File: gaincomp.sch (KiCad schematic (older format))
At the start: 22 parts

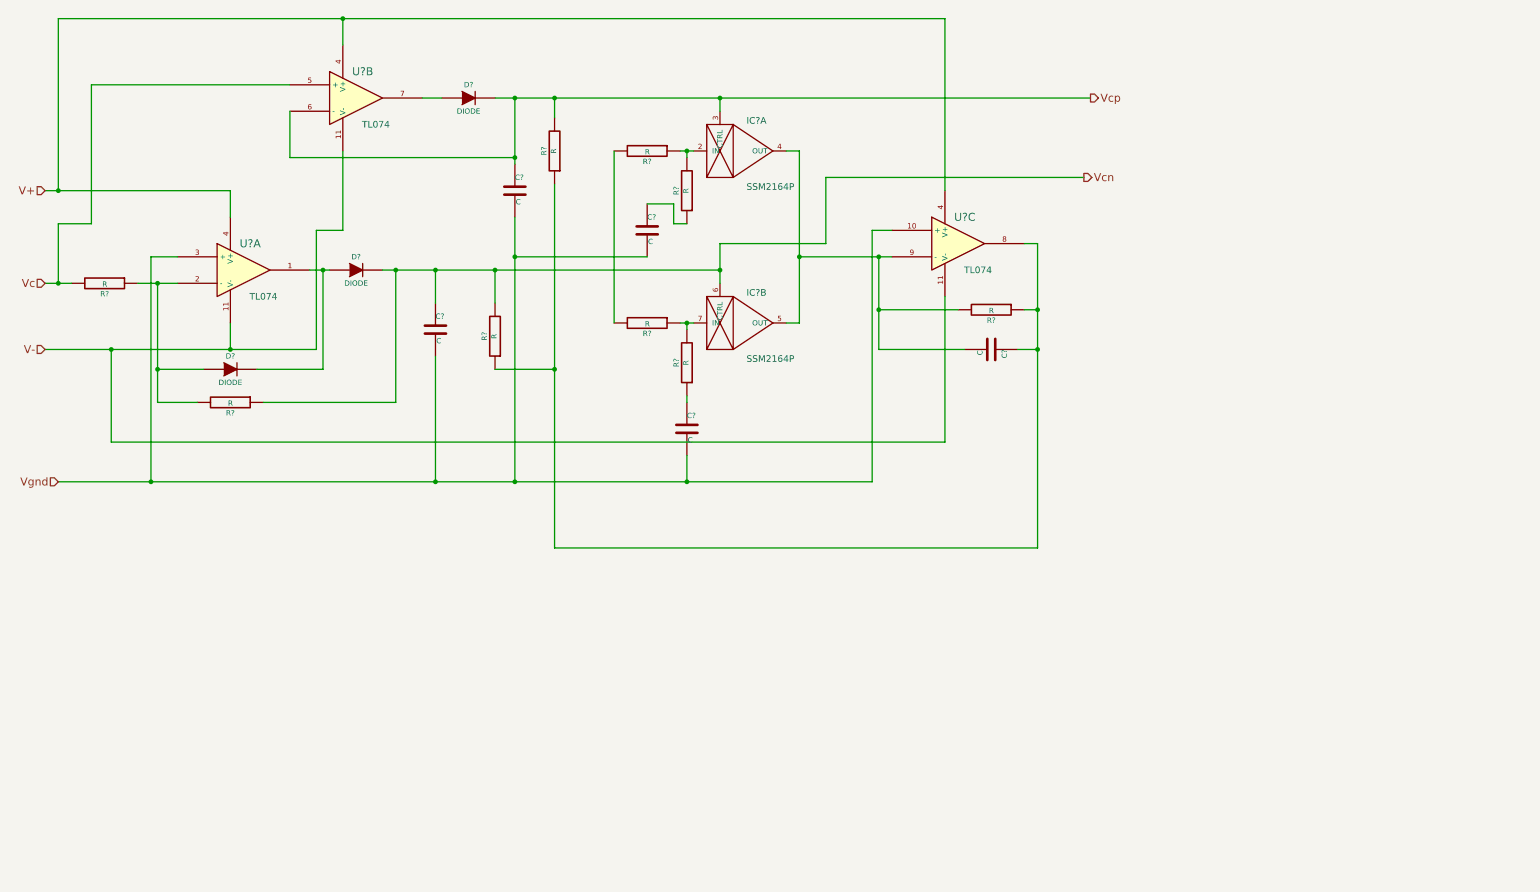
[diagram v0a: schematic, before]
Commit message: Added top-level connections
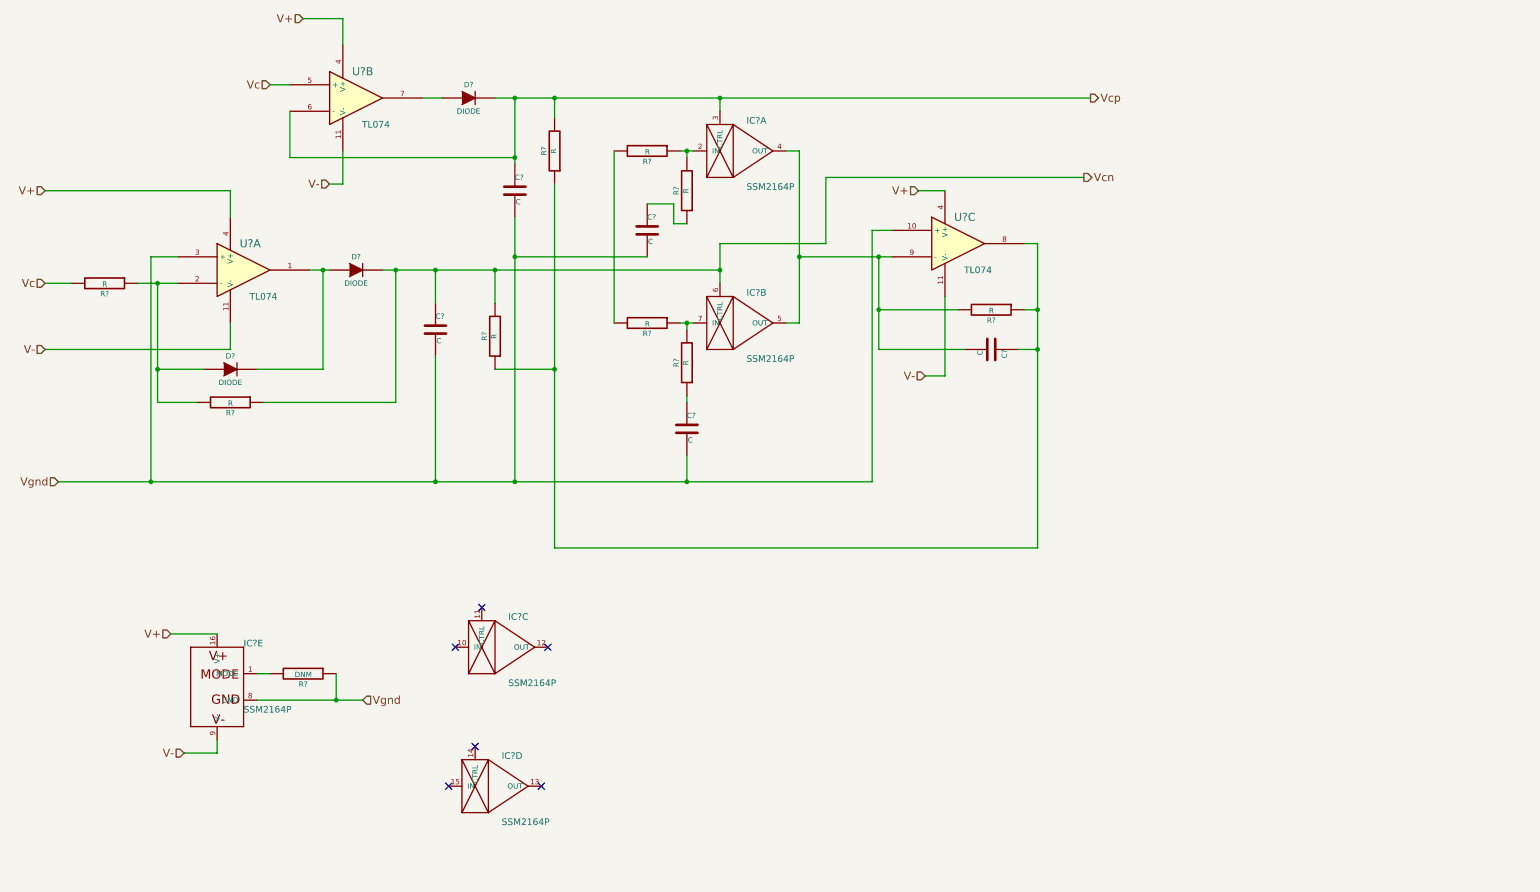
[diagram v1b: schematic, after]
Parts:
- added IC? (x3): SSM2164P, ssm2164-DIL16, symbol SSM2164P
- added R?: DNM, symbol R
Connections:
- net V+: now also IC?.16 (V+)
- net V-: now also IC?.9 (V-)
- net Vgnd: now also IC?.8 (GND), R?.1
- new net: IC?.1 (MODE), R?.2
- no-connect marks 0 -> 6
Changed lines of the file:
@@
 $Descr A4 11693 8268
 encoding utf-8
-Sheet 4 6
+Sheet 4 9
 Title ""
 Date ""
@@
 	2600 2000 2600 2200
 Wire Wire Line
-	1200 3200 3250 3200
-Wire Wire Line
 	2600 3200 2600 3000
 Wire Wire Line
@@
 	1200 2700 1400 2700
 Wire Wire Line
-	1300 2000 1300 700
-Wire Wire Line
 	3450 700  3450 900
-Connection ~ 1300 2000
-Wire Wire Line
-	3250 3200 3250 2300
-Wire Wire Line
-	3250 2300 3450 2300
-Wire Wire Line
-	3450 2300 3450 1700
-Connection ~ 2600 3200
-Wire Wire Line
-	1300 2700 1300 2250
-Wire Wire Line
-	1300 2250 1550 2250
-Wire Wire Line
-	1550 2250 1550 1200
-Wire Wire Line
-	1550 1200 3050 1200
-Connection ~ 1300 2700
 Wire Wire Line
 	4050 1300 4200 1300
@@
 Wire Wire Line
 	6900 3000 6800 3000
-Wire Wire Line
-	8000 700  8000 2000
-Connection ~ 3450 700
-Wire Wire Line
-	8000 2800 8000 3900
-Wire Wire Line
-	8000 3900 1700 3900
-Wire Wire Line
-	1700 3900 1700 3200
-Connection ~ 1700 3200
 Wire Wire Line
 	7600 2500 6900 2500
@@
 Connection ~ 5050 3350
 Connection ~ 8700 3200
-Wire Wire Line
-	1300 700  8000 700
 Connection ~ 6300 1300
 Wire Wire Line
@@
 Wire Wire Line
 	5500 1700 5500 3000
+Text HLabel 2900 1200 0    60   Input ~ 0
+Vc
+Wire Wire Line
+	2900 1200 3050 1200
+Text HLabel 7850 3400 0    60   Input ~ 0
+V-
+Wire Wire Line
+	7850 3400 8000 3400
+Wire Wire Line
+	8000 3400 8000 2800
+Wire Wire Line
+	1200 3200 2600 3200
+Text HLabel 3350 1950 0    60   Input ~ 0
+V-
+Wire Wire Line
+	3350 1950 3450 1950
+Wire Wire Line
+	3450 1950 3450 1700
+Text HLabel 3150 700  0    60   Input ~ 0
+V+
+Wire Wire Line
+	3150 700  3450 700
+Text HLabel 7800 2000 0    60   Input ~ 0
+V+
+Wire Wire Line
+	7800 2000 8000 2000
+$Comp
+L SSM2164P IC?
+U 3 1 5462C12D
+P 4500 5450
+F 0 "IC?" H 4700 5650 50  0000 L BNN
+F 1 "SSM2164P" H 4700 5150 50  0000 L BNN
+F 2 "ssm2164-DIL16" H 4500 5600 50  0001 C CNN
+F 3 "" H 4500 5450 60  0000 C CNN
+	3    4500 5450
+	1    0    0    -1
+$EndComp
+$Comp
+L SSM2164P IC?
+U 4 1 5462C1A4
+P 4450 6500
+F 0 "IC?" H 4650 6700 50  0000 L BNN
+F 1 "SSM2164P" H 4650 6200 50  0000 L BNN
+F 2 "ssm2164-DIL16" H 4450 6650 50  0001 C CNN
+F 3 "" H 4450 6500 60  0000 C CNN
+	4    4450 6500
+	1    0    0    -1
+$EndComp
+$Comp
+L SSM2164P IC?
+U 5 1 5462C219
+P 2500 5650
+F 0 "IC?" H 2700 5850 50  0000 L BNN
+F 1 "SSM2164P" H 2700 5350 50  0000 L BNN
+F 2 "ssm2164-DIL16" H 2500 5800 50  0001 C CNN
+F 3 "" H 2500 5650 60  0000 C CNN
+	5    2500 5650
+	1    0    0    -1
+$EndComp
+Text HLabel 3600 5850 2    60   Input ~ 0
+Vgnd
+Text HLabel 2250 6250 0    60   Input ~ 0
+V-
+Text HLabel 2150 5350 0    60   Input ~ 0
+V+
+Wire Wire Line
+	2150 5350 2500 5350
+Wire Wire Line
+	2250 6250 2500 6250
+Wire Wire Line
+	2500 6250 2500 6150
+Wire Wire Line
+	2800 5850 3600 5850
+NoConn ~ 4300 5450
+NoConn ~ 4500 5150
+NoConn ~ 5000 5450
+NoConn ~ 4950 6500
+NoConn ~ 4450 6200
+NoConn ~ 4250 6500
+$Comp
+L R R?
+U 1 1 5462C5A9
+P 3150 5650
+F 0 "R?" V 3230 5650 40  0000 C CNN
+F 1 "DNM" V 3157 5651 40  0000 C CNN
+F 2 "" V 3080 5650 30  0000 C CNN
+F 3 "" H 3150 5650 30  0000 C CNN
+	1    3150 5650
+	0    1    1    0
+$EndComp
+Wire Wire Line
+	3400 5650 3400 5850
+Connection ~ 3400 5850
+Wire Wire Line
+	2900 5650 2800 5650
 $EndSCHEMATC

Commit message: Some work
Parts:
- removed C? (x5): C, symbol C
- removed D? (x3): DIODE, symbol DIODE
- removed IC? (x3): SSM2164P, ssm2164-DIL16, symbol SSM2164P
- removed R? (x9): R, symbol R
- removed U? (x3): TL074, symbol TL074
- added C? (x2): C, symbol C
- added C? (x2): 560p, symbol C
- added C?: 100p, symbol C
- added D? (x3): DIODE, symbol DIODE
- added IC? (x3): SSM2164P, ssm2164-DIL16, symbol SSM2164P
- added R? (x2): 100k, symbol R
- added R? (x3): 80k, symbol R
- added R? (x2): 500, symbol R
- added R? (x3): 33k, symbol R
- added U? (x5): TL074, symbol TL074
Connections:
- net V+: now also IC?.16 (V+), R?.1, U?.4 (V+), U?.4 (V+), U?.4 (V+), U?.4 (V+), U?.4 (V+)
- net V-: now also IC?.9 (V-), R?.2, R?.2, U?.11 (V-), U?.11 (V-), U?.11 (V-), U?.11 (V-), U?.11 (V-)
- net Vc: now also R?.2, U?.5 (+)
- net Vcn: now also IC?.6 (CTRL), U?.13 (-), U?.14
- net Vcp: now also IC?.3 (CTRL), U?.1, U?.2 (-)
- net Vgnd: now also C?.2, C?.2, C?.2, C?.2, IC?.8 (GND), U?.10 (+), U?.5 (+)
- net at R?.2: now also IC?.1 (MODE)
- new net: C?.1, D?.2 (K), R?.2, U?.3 (+), U?.6 (-)
- new net: D?.1 (A), U?.7
- new net: D?.1 (A), R?.1, R?.2, U?.9 (-)
- new net: D?.1 (A), D?.2 (K), U?.8
- new net: C?.1, D?.2 (K), R?.1, R?.2, U?.12 (+)
- new net: C?.1, R?.1 (x2)
- new net: IC?.2 (IN), R?.1, R?.2
- new net: C?.2, IC?.4 (OUT), IC?.5 (OUT), R?.2, R?.2, U?.6 (-)
- new net: IC?.7 (IN), R?.1, R?.2
- new net vo: C?.1, R?.1, R?.1, R?.1, U?.7
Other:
- note added: "This resistor adds bias current, so that when the gain is 1, the\ncurrent seen by the amp below is 0.\nio = ii * 10^(-2/3vc)"
- note added: "When used as feedback, the gain here can be\nincreased (increase the 33k resistor)."
- note added: "vo > 0V"
- moved on the sheet: IC?C, IC?D, R?

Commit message: Ready for tapeout
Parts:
- added R15, R16: 100k, symbol R
- R17, R18: renamed from R?; value 33k -> 100k
- gave numbers to parts that had none: 20
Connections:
- net Vcn: now also U4.1, U4.2 (-); no longer U4.13 (-), U4.14
- net Vcp: now also U1.13 (-), U1.14; no longer U1.1, U1.2 (-)
- net at C19.1, D3.2 (K), U1.6 (-): now also R15.1; no longer R17.2, U1.3 (+)
- net at C20.1, D4.2 (K), R13.1: now also R16.1; no longer R18.2, U4.12 (+)
- new net: R15.2, R17.2, U1.12 (+)
- new net: R16.2, R18.2, U4.3 (+)
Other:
- note added: "-10V to +10V"
- note added: "This resistor adds bias current, so that when the gain is 1, the\ncurrent seen by the amp below is 0.\nio = ii * 10^(-2/3vc). Increase resistor to lower gain."
- note removed: "This resistor adds bias current, so that when the gain is 1, the\ncurrent seen by the amp below is 0.\nio = ii * 10^(-2/3vc)"
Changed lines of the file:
@@
 $Descr A4 11693 8268
 encoding utf-8
-Sheet 4 9
+Sheet 4 10
 Title ""
 Date ""
@@
 Vcn
 $Comp
-L SSM2164P IC?
+L SSM2164P IC1
 U 3 1 5462C12D
 P 3050 6900
-F 0 "IC?" H 3250 7100 50  0000 L BNN
+F 0 "IC1" H 3250 7100 50  0000 L BNN
 F 1 "SSM2164P" H 3250 6600 50  0000 L BNN
 F 2 "ssm2164-DIL16" H 3050 7050 50  0001 C CNN
@@
 $EndComp
 $Comp
-L SSM2164P IC?
+L SSM2164P IC1
 U 4 1 5462C1A4
 P 5100 6650
-F 0 "IC?" H 5300 6850 50  0000 L BNN
+F 0 "IC1" H 5300 6850 50  0000 L BNN
 F 1 "SSM2164P" H 5300 6350 50  0000 L BNN
 F 2 "ssm2164-DIL16" H 5100 6800 50  0001 C CNN
@@
 NoConn ~ 4900 6650
 $Comp
-L R R?
+L R R14
 U 1 1 5462C5A9
 P 3800 5800
-F 0 "R?" V 3880 5800 40  0000 C CNN
+F 0 "R14" V 3880 5800 40  0000 C CNN
 F 1 "DNM" V 3807 5801 40  0000 C CNN
 F 2 "" V 3730 5800 30  0000 C CNN
@@
 $EndComp
 $Comp
-L TL074 U?
+L TL074 U1
 U 2 1 54A69C55
 P 2850 1550
-F 0 "U?" H 2900 1750 60  0000 C CNN
+F 0 "U1" H 2900 1750 60  0000 C CNN
 F 1 "TL074" H 3000 1350 50  0000 C CNN
 F 2 "" H 2850 1550 60  0000 C CNN
@@
 $EndComp
 $Comp
-L DIODE D?
+L DIODE D3
 U 1 1 54A69C67
 P 3750 1550
-F 0 "D?" H 3750 1650 40  0000 C CNN
+F 0 "D3" H 3750 1650 40  0000 C CNN
 F 1 "DIODE" H 3750 1450 40  0000 C CNN
 F 2 "" H 3750 1550 60  0000 C CNN
@@
 $EndComp
 $Comp
-L R R?
+L R R12
 U 1 1 54A69D4C
 P 1900 3250
-F 0 "R?" V 1980 3250 40  0000 C CNN
+F 0 "R12" V 1980 3250 40  0000 C CNN
 F 1 "100k" V 1907 3251 40  0000 C CNN
 F 2 "" V 1830 3250 30  0000 C CNN
@@
 V-
 $Comp
-L DIODE D?
+L DIODE D2
 U 1 1 54A69FAB
 P 2750 4100
-F 0 "D?" H 2750 4200 40  0000 C CNN
+F 0 "D2" H 2750 4200 40  0000 C CNN
 F 1 "DIODE" H 2750 4000 40  0000 C CNN
 F 2 "" H 2750 4100 60  0000 C CNN
@@
 $EndComp
 $Comp
-L R R?
+L R R13
 U 1 1 54A69FBB
 P 2750 4350
-F 0 "R?" V 2830 4350 40  0000 C CNN
+F 0 "R13" V 2830 4350 40  0000 C CNN
 F 1 "100k" V 2757 4351 40  0000 C CNN
 F 2 "" V 2680 4350 30  0000 C CNN
@@
 Vgnd
 $Comp
-L DIODE D?
+L DIODE D4
 U 1 1 54A6A594
 P 3750 3150
-F 0 "D?" H 3750 3250 40  0000 C CNN
+F 0 "D4" H 3750 3250 40  0000 C CNN
 F 1 "DIODE" H 3750 3050 40  0000 C CNN
 F 2 "" H 3750 3150 60  0000 C CNN
@@
 $EndComp
 $Comp
-L C C?
+L C C19
 U 1 1 54A6A72C
 P 4250 1850
-F 0 "C?" H 4250 1950 40  0000 L CNN
+F 0 "C19" H 4250 1950 40  0000 L CNN
 F 1 "C" H 4256 1765 40  0000 L CNN
 F 2 "" H 4288 1700 30  0000 C CNN
@@
 Vgnd
 $Comp
-L C C?
+L C C22
 U 1 1 54A6A84D
 P 7850 4450
-F 0 "C?" H 7850 4550 40  0000 L CNN
+F 0 "C22" H 7850 4550 40  0000 L CNN
 F 1 "560p" H 7856 4365 40  0000 L CNN
 F 2 "" H 7888 4300 30  0000 C CNN
@@
 $EndComp
 $Comp
-L SSM2164P IC?
+L SSM2164P IC1
 U 1 1 54A6AEA4
 P 8150 1950
-F 0 "IC?" H 8350 2150 50  0000 L BNN
+F 0 "IC1" H 8350 2150 50  0000 L BNN
 F 1 "SSM2164P" H 8350 1650 50  0000 L BNN
 F 2 "ssm2164-DIL16" H 8150 2100 50  0001 C CNN
@@
 $EndComp
 $Comp
-L SSM2164P IC?
+L SSM2164P IC1
 U 2 1 54A6AEAF
 P 8150 3550
-F 0 "IC?" H 8350 3750 50  0000 L BNN
+F 0 "IC1" H 8350 3750 50  0000 L BNN
 F 1 "SSM2164P" H 8350 3250 50  0000 L BNN
 F 2 "ssm2164-DIL16" H 8150 3700 50  0001 C CNN
@@
 $EndComp
 $Comp
-L R R?
+L R R19
 U 1 1 54A6B133
 P 7500 1950
-F 0 "R?" V 7580 1950 40  0000 C CNN
+F 0 "R19" V 7580 1950 40  0000 C CNN
 F 1 "80k" V 7507 1951 40  0000 C CNN
 F 2 "" V 7430 1950 30  0000 C CNN
@@
 $EndComp
 $Comp
-L R R?
+L R R21
 U 1 1 54A6B13E
 P 7850 2300
-F 0 "R?" V 7930 2300 40  0000 C CNN
+F 0 "R21" V 7930 2300 40  0000 C CNN
 F 1 "500" V 7857 2301 40  0000 C CNN
 F 2 "" V 7780 2300 30  0000 C CNN
@@
 $EndComp
 $Comp
-L R R?
+L R R20
 U 1 1 54A6B149
 P 7500 3550
-F 0 "R?" V 7580 3550 40  0000 C CNN
+F 0 "R20" V 7580 3550 40  0000 C CNN
 F 1 "80k" V 7507 3551 40  0000 C CNN
 F 2 "" V 7430 3550 30  0000 C CNN
@@
 $EndComp
 $Comp
-L R R?
+L R R22
 U 1 1 54A6B154
 P 7850 3900
-F 0 "R?" V 7930 3900 40  0000 C CNN
+F 0 "R22" V 7930 3900 40  0000 C CNN
 F 1 "500" V 7857 3901 40  0000 C CNN
 F 2 "" V 7780 3900 30  0000 C CNN
@@
 $EndComp
 $Comp
-L C C?
+L C C21
 U 1 1 54A6B15F
 P 7850 2850
-F 0 "C?" H 7850 2950 40  0000 L CNN
+F 0 "C21" H 7850 2950 40  0000 L CNN
 F 1 "560p" H 7856 2765 40  0000 L CNN
 F 2 "" H 7888 2700 30  0000 C CNN
@@
 $EndComp
 $Comp
-L C C?
+L C C20
 U 1 1 54A6B16A
 P 4250 3450
-F 0 "C?" H 4250 3550 40  0000 L CNN
+F 0 "C20" H 4250 3550 40  0000 L CNN
 F 1 "C" H 4256 3365 40  0000 L CNN
 F 2 "" H 4288 3300 30  0000 C CNN
@@
 Vgnd
 $Comp
-L TL074 U?
+L TL074 U1
 U 3 1 54A6B66B
 P 2850 3150
-F 0 "U?" H 2900 3350 60  0000 C CNN
+F 0 "U1" H 2900 3350 60  0000 C CNN
 F 1 "TL074" H 3000 2950 50  0000 C CNN
 F 2 "" H 2850 3150 60  0000 C CNN
@@
 Vgnd
 $Comp
-L R R?
+L R R24
 U 1 1 54A6BB31
 P 9900 4300
-F 0 "R?" V 9980 4300 40  0000 C CNN
+F 0 "R24" V 9980 4300 40  0000 C CNN
 F 1 "33k" V 9907 4301 40  0000 C CNN
 F 2 "" V 9830 4300 30  0000 C CNN
@@
 $EndComp
 $Comp
-L C C?
+L C C23
 U 1 1 54A6BB3C
 P 9900 4550
-F 0 "C?" V 10050 4550 40  0000 L CNN
+F 0 "C23" V 10050 4550 40  0000 L CNN
 F 1 "100p" V 9850 4650 40  0000 L CNN
 F 2 "" H 9938 4400 30  0000 C CNN
@@
 $EndComp
 $Comp
-L R R?
+L R R23
 U 1 1 54A6CBE5
 P 9200 1950
-F 0 "R?" V 9280 1950 40  0000 C CNN
+F 0 "R23" V 9280 1950 40  0000 C CNN
 F 1 "80k" V 9207 1951 40  0000 C CNN
 F 2 "" V 9130 1950 30  0000 C CNN
@@
 When used as feedback, the gain here can be\nincreased (increase the 33k resistor).
 Text Notes 8800 1800 0    60   ~ 0
-This resistor adds bias current, so that when the gain is 1, the\ncurrent seen by the amp below is 0.\nio = ii * 10^(-2/3vc)
+This resistor adds bias current, so that when the gain is 1, the\ncurrent seen by the amp below is 0.\nio = ii * 10^(-2/3vc). Increase resistor to lower gain.
 Text HLabel 9550 1950 2    60   Input ~ 0
 V+
@@
 V-
 $Comp
-L SSM2164P IC?
+L SSM2164P IC1
 U 5 1 54A92775
 P 3150 5800
-F 0 "IC?" H 3350 6000 50  0000 L BNN
+F 0 "IC1" H 3350 6000 50  0000 L BNN
 F 1 "SSM2164P" H 3350 5500 50  0000 L BNN
 F 2 "ssm2164-DIL16" H 3150 5950 50  0001 C CNN
@@
 V+
 $Comp
-L TL074 U?
-U 1 1 54A965B4
+L TL074 U1
+U 4 1 54A965B4
 P 6250 1550
-F 0 "U?" H 6300 1750 60  0000 C CNN
+F 0 "U1" H 6300 1750 60  0000 C CNN
 F 1 "TL074" H 6400 1350 50  0000 C CNN
 F 2 "" H 6250 1550 60  0000 C CNN
 F 3 "" H 6250 1550 60  0000 C CNN
-	1    6250 1550
-	1    0    0    -1
-$EndComp
-$Comp
-L TL074 U?
-U 4 1 54A965C8
+	4    6250 1550
+	1    0    0    -1
+$EndComp
+$Comp
+L TL074 U4
+U 1 1 54A965C8
 P 6250 3150
-F 0 "U?" H 6300 3350 60  0000 C CNN
+F 0 "U4" H 6300 3350 60  0000 C CNN
 F 1 "TL074" H 6400 2950 50  0000 C CNN
 F 2 "" H 6250 3150 60  0000 C CNN
 F 3 "" H 6250 3150 60  0000 C CNN
-	4    6250 3150
+	1    6250 3150
 	1    0    0    -1
 $EndComp
@@
 V-
 $Comp
-L R R?
+L R R17
 U 1 1 54A9638B
 P 4600 1900
-F 0 "R?" V 4680 1900 40  0000 C CNN
-F 1 "33k" V 4607 1901 40  0000 C CNN
+F 0 "R17" V 4680 1900 40  0000 C CNN
+F 1 "100k" V 4607 1901 40  0000 C CNN
 F 2 "" V 4530 1900 30  0000 C CNN
 F 3 "" H 4600 1900 30  0000 C CNN
@@
 	-1   0    0    1
 $EndComp
+$Comp
+L R R18
+U 1 1 54B11176
+P 4600 3500
+F 0 "R18" V 4680 3500 40  0000 C CNN
+F 1 "100k" V 4607 3501 40  0000 C CNN
+F 2 "" V 4530 3500 30  0000 C CNN
+F 3 "" H 4600 3500 30  0000 C CNN
+	1    4600 3500
+	-1   0    0    1
+$EndComp
+Text HLabel 7150 3550 0    60   Input ~ 0
+V-
+$Comp
+L TL074 U4
+U 2 1 54FF9680
+P 10000 3450
+F 0 "U4" H 10050 3650 60  0000 C CNN
+F 1 "TL074" H 10150 3250 50  0000 C CNN
+F 2 "" H 10000 3450 60  0000 C CNN
+F 3 "" H 10000 3450 60  0000 C CNN
+	2    10000 3450
+	1    0    0    -1
+$EndComp
+$Comp
+L R R15
+U 1 1 5504F2C8
+P 4350 1200
+F 0 "R15" V 4430 1200 40  0000 C CNN
+F 1 "100k" V 4357 1201 40  0000 C CNN
+F 2 "" V 4280 1200 30  0000 C CNN
+F 3 "" H 4350 1200 30  0000 C CNN
+	1    4350 1200
+	0    -1   -1   0
+$EndComp
+$Comp
+L R R16
+U 1 1 5504F422
+P 4350 2900
+F 0 "R16" V 4430 2900 40  0000 C CNN
+F 1 "100k" V 4357 2901 40  0000 C CNN
+F 2 "" V 4280 2900 30  0000 C CNN
+F 3 "" H 4350 2900 30  0000 C CNN
+	1    4350 2900
+	0    -1   -1   0
+$EndComp
 Wire Wire Line
 	2900 6400 3150 6400
@@
 	4250 3150 4250 3250
 Connection ~ 4050 3150
-Connection ~ 4250 1550
-Connection ~ 4250 3150
 Wire Wire Line
 	8150 1550 8150 1650
@@
 	9550 1950 9450 1950
 Wire Wire Line
-	3950 1550 5050 1550
-Wire Wire Line
-	10500 4850 10500 3450
+	3950 1550 4250 1550
+Wire Wire Line
+	10500 3450 10500 4850
 Wire Wire Line
 	3150 5400 3150 5500
@@
 Connection ~ 1550 1450
 Wire Wire Line
-	4600 1650 4600 1550
-Connection ~ 4600 1550
-Wire Wire Line
 	6150 2050 6150 1950
 Wire Wire Line
@@
 	6750 3150 8450 3150
 Wire Wire Line
-	3950 3150 5050 3150
-Wire Wire Line
-	4750 4850 10500 4850
-Wire Wire Line
-	5050 3050 5750 3050
+	3950 3150 4250 3150
+Wire Wire Line
+	10500 4850 4750 4850
 Connection ~ 6850 3150
 Wire Wire Line
 	6750 1550 8450 1550
 Wire Wire Line
-	5050 1450 5750 1450
-$Comp
-L R R?
-U 1 1 54B11176
-P 4600 3500
-F 0 "R?" V 4680 3500 40  0000 C CNN
-F 1 "33k" V 4607 3501 40  0000 C CNN
-F 2 "" V 4530 3500 30  0000 C CNN
-F 3 "" H 4600 3500 30  0000 C CNN
-	1    4600 3500
-	-1   0    0    1
-$EndComp
-Wire Wire Line
-	5050 1550 5050 1450
-Wire Wire Line
 	6850 3150 6850 3900
 Wire Wire Line
@@
 Wire Wire Line
 	5650 3250 5750 3250
-Wire Wire Line
-	5050 3150 5050 3050
-Wire Wire Line
-	4600 3250 4600 3150
-Connection ~ 4600 3150
 Wire Wire Line
 	4600 2150 4750 2150
@@
 	6850 2350 6850 1550
 Connection ~ 6850 1550
-Text HLabel 7150 3550 0    60   Input ~ 0
-V-
-$Comp
-L TL074 U?
-U 2 1 54FF9680
-P 10000 3450
-F 0 "U?" H 10050 3650 60  0000 C CNN
-F 1 "TL074" H 10150 3250 50  0000 C CNN
-F 2 "" H 10000 3450 60  0000 C CNN
-F 3 "" H 10000 3450 60  0000 C CNN
-	2    10000 3450
-	1    0    0    -1
-$EndComp
+Wire Wire Line
+	4100 1200 4100 1550
+Connection ~ 4100 1550
+Wire Wire Line
+	4600 1200 4600 1650
+Wire Wire Line
+	5750 1450 4600 1450
+Connection ~ 4600 1450
+Wire Wire Line
+	4100 3150 4100 2900
+Connection ~ 4100 3150
+Wire Wire Line
+	4600 2900 4600 3250
+Wire Wire Line
+	5750 3050 4600 3050
+Connection ~ 4600 3050
+Text Notes 1700 1350 2    60   ~ 0
+-10V to +10V
 $EndSCHEMATC
